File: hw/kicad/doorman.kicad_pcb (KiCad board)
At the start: 2 copper layers, 18 parts, among them J1 Ring Detection, J2 Lock, J3 Power Supply, K1 S1A05, Q1 BC337, SW1 Button, U1 WeMos_mini, U2 PC817

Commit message: New Dorman v 1.0 PCB design.
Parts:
- added H1: MountingHole_2.2mm_M2, MountingHole:MountingHole_2.2mm_M2, F.Cu at (126.0, 117.0)
- added H1: MountingHole_2.2mm_M2, MountingHole:MountingHole_2.2mm_M2, F.Cu at (104.0, 66.0)
- Button: renamed from SW1; footprint Button_Switch_SMD:SW_SPST_EVQP0 -> Connector_PinHeader_2.54mm:PinHeader_1x02_P2.54mm_Vertical
- J1: value Ring Detection -> RDet
- J3: value Power Supply -> PWR
- LockLED: renamed from LED2; value LED Red -> Red
- R1, R2, R3, R4, R5: footprint Resistor_THT:R_Axial_DIN0204_L3.6mm_D1.6mm_P5.08mm_Vertical -> Resistor_THT:R_Axial_DIN0204_L3.6mm_D1.6mm_P7.62mm_Horizontal
- RingLED: renamed from LED1; value LED Green -> Green
- U1: value WeMos_mini -> WeMos_D1_mini
- moved J1 77.2 mm to (111.3, 127.8), turned to 180 degrees
- moved R3 71.6 mm to (108.7, 66.5), turned to 270 degrees
- moved D1 66.3 mm to (109.2, 112.3), turned to 270 degrees
- moved J3 62.8 mm to (113.8, 54.9)
- moved LockLED 57.1 mm to (111.3, 62.7), turned to 180 degrees
- moved JP1 54.1 mm to (108.5, 54.9), turned to 270 degrees
- moved K1 52.7 mm to (122.9, 105.7), turned to 180 degrees
- moved J2 47.7 mm to (119.9, 127.8), turned to 180 degrees
- moved RingLED 41.5 mm to (120.9, 62.7)
- moved U2 41.4 mm to (119.6, 93.0), turned to 90 degrees
- moved D2 41.3 mm to (111.3, 100.3)
- moved R2 40.4 mm to (123.4, 66.5), turned to 270 degrees
- moved R4 32.6 mm to (107.4, 82.8), turned to 270 degrees
- moved Q1 32.4 mm to (112.5, 82.8), turned to 270 degrees
- moved R5 28.5 mm to (115.1, 93.0), turned to 180 degrees
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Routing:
- net GND: track 0.00 -> 126.0 mm
- net +5V: track 0.00 -> 59.0 mm
- net PhGND: track 0.00 -> 56.3 mm
- net Net-(D2-Pad2): track 0.00 -> 54.9 mm
- net PhLock: track 0.00 -> 40.0 mm
- net Net-(D1-Pad1): track 0.00 -> 27.7 mm
- net Net-(R2-Pad2): track 0.00 -> 26.7 mm
- net Butt: track 0.00 -> 24.1 mm
- net PhRing: track 0.00 -> 10.4 mm
- net +3V3: track 0.00 -> 9.67 mm
- net Net-(Q1-Pad2): track 0.00 -> 6.13 mm
- net Net-(J3-Pad1): track 0.00 -> 5.33 mm
- net Net-(LED2-Pad2): track 0.00 -> 3.81 mm
- net Net-(LED1-Pad2): track 0.00 -> 3.81 mm
- net RingDet: track 0.00 -> 3.81 mm
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- added copper zone on F.Cu, net GND
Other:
- board outline added: 28 x 80 mm
- net class My added: clearance 0.2, trace_width 0.35, via_dia 0.8, via_drill 0.4
- board text added: "+"
- board text added: "-"
- board text added: "Doorman HomeKit"
- board text added: "Ext PWR"
- board text added: "Lock"
- board text added: "Only +5V"
- board text added: "RingDet"
- board text added: "version 1.0"
- board text added: "zokl@2020"

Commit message: PCB Update.
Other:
- net class My removed
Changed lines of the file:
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@@
     (visible_elements FFFFFF7F)
     (pcbplotparams
-      (layerselection 0x010fc_ffffffff)
+      (layerselection 0x010a0_7fffffff)
       (usegerberextensions false)
       (usegerberattributes false)
@@
       (padsonsilk false)
       (subtractmaskfromsilk false)
-      (outputformat 1)
+      (outputformat 4)
       (mirror false)
-      (drillshape 1)
+      (drillshape 0)
       (scaleselection 1)
       (outputdirectory ""))
@@
     (add_net PhRing)
     (add_net RingDet)
-  )
-  (net_class My ""
-    (clearance 0.2)
-    (trace_width 0.35)
-    (via_dia 0.8)
-    (via_drill 0.4)
-    (uvia_dia 0.3)
-    (uvia_drill 0.1)
   )
   (module Package_TO_SOT_THT:TO-92_Inline_Wide (layer F.Cu)
@@
     (connect_pads (clearance 0.508))
     (min_thickness 0.254)
-    (fill (arc_segments 32) (thermal_gap 0.508) (thermal_bridge_width 0.508))
+    (fill yes (arc_segments 32) (thermal_gap 0.508) (thermal_bridge_width 0.508))
     (polygon
       (pts

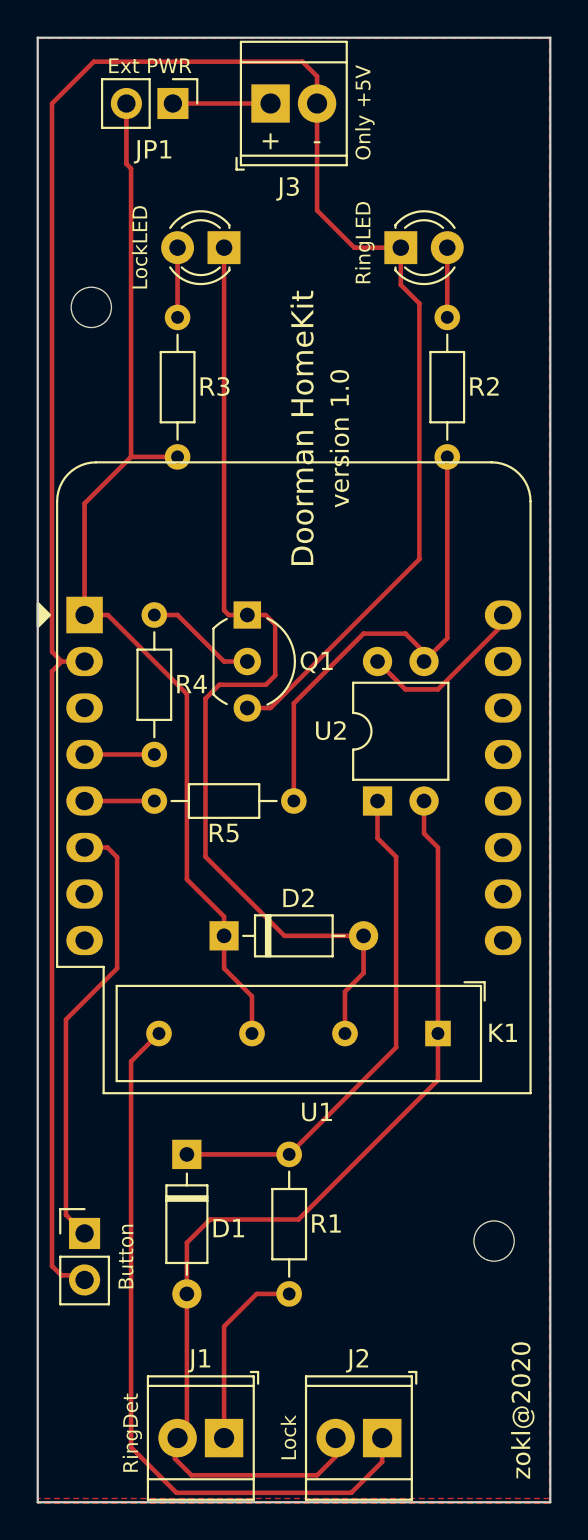
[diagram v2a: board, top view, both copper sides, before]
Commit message: New PCB mask, new PWR wires size.
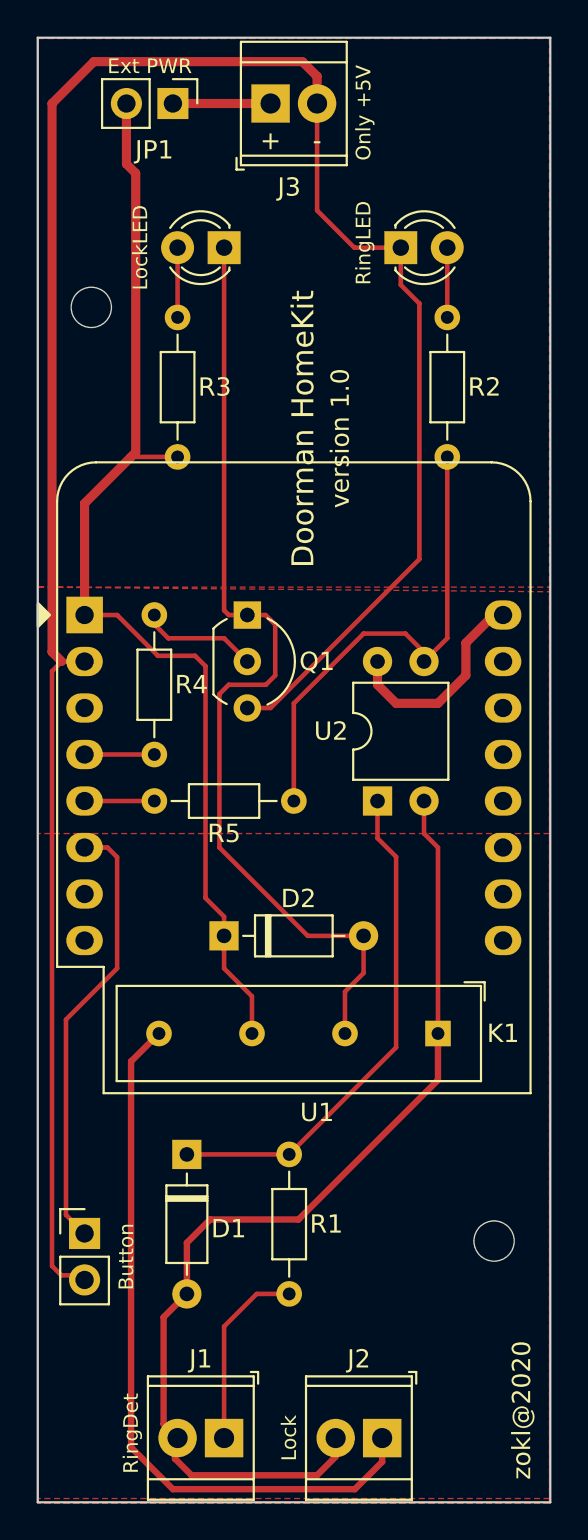
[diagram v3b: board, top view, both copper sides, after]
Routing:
- net +3V3: track 9.67 -> 11.8 mm
- net +5V: track 59.0 -> 60.7 mm
- net Net-(D2-Pad2): track 54.9 -> 53.2 mm

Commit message: Final PCB.
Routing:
- net +5V: track 60.7 -> 61.7 mm
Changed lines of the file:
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@@
-(kicad_pcb (version 20171130) (host pcbnew "(5.1.5-0-10_14)")
+(kicad_pcb (version 20171130) (host pcbnew 5.1.5-52549c5~84~ubuntu18.04.1)
   (general
     (thickness 1.6)
     (drawings 19)
-    (tracks 112)
+    (tracks 115)
     (zones 0)
     (modules 20)
@@
     (last_trace_width 0.25)
     (trace_clearance 0.2)
-    (zone_clearance 0.508)
+    (zone_clearance 0.48)
     (zone_45_only no)
     (trace_min 0.2)
@@
     (solder_mask_min_width 0.25)
     (aux_axis_origin 0 0)
+    (grid_origin 101.072 51.27)
     (visible_elements FFFFFF7F)
     (pcbplotparams
@@
   (segment (start 111.252 100.33) (end 111.252 102.108) (width 0.25) (layer F.Cu) (net 4))
   (segment (start 111.252 102.108) (end 112.776 103.632) (width 0.25) (layer F.Cu) (net 4))
-  (segment (start 106.172 74.168) (end 108.712 74.168) (width 0.25) (layer F.Cu) (net 4))
-  (segment (start 103.632 76.708) (end 106.172 74.168) (width 0.5) (layer F.Cu) (net 4))
-  (segment (start 103.632 82.804) (end 103.632 76.708) (width 0.5) (layer F.Cu) (net 4))
-  (segment (start 106.426 73.914) (end 106.172 74.168) (width 0.5) (layer F.Cu) (net 4))
-  (segment (start 106.426 58.674) (end 106.426 73.914) (width 0.5) (layer F.Cu) (net 4))
-  (segment (start 105.918 58.166) (end 106.426 58.674) (width 0.5) (layer F.Cu) (net 4))
-  (segment (start 105.918 54.864) (end 105.918 58.166) (width 0.5) (layer F.Cu) (net 4))
+  (segment (start 107.188 64.262) (end 107.188 73.152) (width 0.5) (layer F.Cu) (net 4))
+  (segment (start 105.918 62.992) (end 107.188 64.262) (width 0.5) (layer F.Cu) (net 4))
+  (segment (start 105.918 54.864) (end 105.918 62.992) (width 0.5) (layer F.Cu) (net 4))
+  (segment (start 107.188 73.914) (end 107.188 73.152) (width 0.5) (layer F.Cu) (net 4))
+  (segment (start 108.458 74.422) (end 108.712 74.168) (width 0.25) (layer F.Cu) (net 4))
+  (segment (start 107.188 74.422) (end 108.458 74.422) (width 0.25) (layer F.Cu) (net 4))
+  (segment (start 107.188 73.914) (end 107.188 74.422) (width 0.25) (layer F.Cu) (net 4))
+  (segment (start 107.188 80.518) (end 107.188 73.914) (width 0.5) (layer F.Cu) (net 4))
+  (segment (start 104.902 82.804) (end 107.188 80.518) (width 0.5) (layer F.Cu) (net 4))
+  (segment (start 103.632 82.804) (end 104.902 82.804) (width 0.5) (layer F.Cu) (net 4))
   (segment (start 111.252 99.28) (end 111.252 100.33) (width 0.25) (layer F.Cu) (net 4))
+  (segment (start 110.236 98.264) (end 111.252 99.28) (width 0.25) (layer F.Cu) (net 4))
+  (segment (start 104.648 82.804) (end 106.87601 85.03201) (width 0.25) (layer F.Cu) (net 4))
   (segment (start 110.236 85.598) (end 110.236 98.264) (width 0.25) (layer F.Cu) (net 4))
-  (segment (start 110.236 98.264) (end 111.252 99.28) (width 0.25) (layer F.Cu) (net 4))
-  (segment (start 103.632 82.804) (end 105.41 82.804) (width 0.25) (layer F.Cu) (net 4))
-  (segment (start 107.63801 85.03201) (end 109.67001 85.03201) (width 0.25) (layer F.Cu) (net 4))
-  (segment (start 105.41 82.804) (end 107.63801 85.03201) (width 0.25) (layer F.Cu) (net 4))
+  (segment (start 106.87601 85.03201) (end 109.67001 85.03201) (width 0.25) (layer F.Cu) (net 4))
   (segment (start 109.67001 85.03201) (end 110.236 85.598) (width 0.25) (layer F.Cu) (net 4))
+  (segment (start 103.632 82.804) (end 104.648 82.804) (width 0.25) (layer F.Cu) (net 4))
   (segment (start 113.03 119.888) (end 114.808 119.888) (width 0.25) (layer F.Cu) (net 5))
   (segment (start 111.252 121.666) (end 113.03 119.888) (width 0.25) (layer F.Cu) (net 5))
@@
   (segment (start 126.492 82.804) (end 125.984 82.804) (width 0.5) (layer F.Cu) (net 16))
   (zone (net 7) (net_name GND) (layer F.Cu) (hatch edge 0.508)
-    (connect_pads (clearance 0.508))
+    (connect_pads (clearance 0.48))
     (min_thickness 0.254)
-    (fill (arc_segments 32) (thermal_gap 0.508) (thermal_bridge_width 0.508))
+    (fill yes (arc_segments 32) (thermal_gap 0.48) (thermal_bridge_width 0.48))
     (polygon
       (pts
-        (xy 129.032 131.064) (xy 101.092 131.064) (xy 101.092 51.308) (xy 129.032 51.308)
+        (xy 129.072 131.27) (xy 101.072 131.27) (xy 101.072 81.67) (xy 129.072 81.67)
       )
     )
-  )
-  (zone (net 7) (net_name GND) (layer F.Cu) (hatch edge 0.508)
-    (connect_pads (clearance 0.508))
-    (min_thickness 0.254)
-    (fill (arc_segments 32) (thermal_gap 0.508) (thermal_bridge_width 0.508))
-    (polygon
-      (pts
-        (xy 129.032 131.318) (xy 101.092 131.318) (xy 101.092 51.308) (xy 129.032 51.308)
-      )
-    )
-  )
-  (zone (net 7) (net_name GND) (layer F.Cu) (hatch edge 0.508)
-    (connect_pads (clearance 0.508))
-    (min_thickness 0.254)
-    (fill (arc_segments 32) (thermal_gap 0.508) (thermal_bridge_width 0.508))
-    (polygon
-      (pts
-        (xy 129.032 131.318) (xy 101.092 131.318) (xy 101.092 51.308) (xy 129.032 51.308)
-      )
-    )
-  )
-  (zone (net 7) (net_name GND) (layer F.Cu) (hatch edge 0.508)
-    (connect_pads (clearance 0.508))
-    (min_thickness 0.254)
-    (fill (arc_segments 32) (thermal_gap 0.508) (thermal_bridge_width 0.508))
-    (polygon
-      (pts
-        (xy 129.032 94.742) (xy 101.092 94.742) (xy 101.092 81.28) (xy 129.032 81.28)
-      )
-    )
-  )
-  (zone (net 7) (net_name GND) (layer F.Cu) (hatch edge 0.508)
-    (connect_pads (clearance 0.508))
-    (min_thickness 0.254)
-    (fill yes (arc_segments 32) (thermal_gap 0.508) (thermal_bridge_width 0.508))
-    (polygon
-      (pts
-        (xy 129.032 81.534) (xy 129.032 131.318) (xy 101.092 131.318) (xy 101.092 81.28)
-      )
-    )

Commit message: PCB production documentation
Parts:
- removed the H1 at (126.0, 117.0)
- removed the H1 at (104.0, 66.0)
- added H1: MountingHole_Pad, MountingHole:MountingHole_2.2mm_M2_Pad, F.Cu at (126.0, 117.0)
- added H2: MountingHole_Pad, MountingHole:MountingHole_2.2mm_M2_Pad, F.Cu at (104.0, 66.0)
- J1: value RDet -> Ring Detection
- J3: value PWR -> Power Supply
- renumbered RingLED to LED1, LockLED to LED2, Button to SW1
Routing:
- net GND: track 126.0 -> 128.1 mm
- added copper zone on B.Cu, net GND
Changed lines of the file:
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@@
     (thickness 1.6)
     (drawings 19)
-    (tracks 115)
+    (tracks 118)
     (zones 0)
     (modules 20)
@@
     (add_net RingDet)
   )
+  (module MountingHole:MountingHole_2.2mm_M2_Pad (layer F.Cu)
+    (at 104 66)
+    (descr "Mounting Hole 2.2mm, M2")
+    (tags "mounting hole 2.2mm m2")
+    (attr virtual)
+    (fp_text reference H2 (at 0 -3.2) (layer F.SilkS) hide
+      (effects (font (size 1 1) (thickness 0.15)))
+    )
+    (fp_text value MountingHole_Pad (at 0 3.2) (layer F.Fab)
+      (effects (font (size 1 1) (thickness 0.15)))
+    )
+    (fp_circle (center 0 0) (end 2.45 0) (layer F.CrtYd) (width 0.05))
+    (fp_circle (center 0 0) (end 2.2 0) (layer Cmts.User) (width 0.15))
+    (fp_text user %R (at 0.3 0) (layer F.Fab)
+      (effects (font (size 1 1) (thickness 0.15)))
+    )
+    (pad 1 thru_hole circle (at 0 0) (size 4.4 4.4) (drill 2.2) (layers *.Cu *.Mask)
+      (net 7 GND))
+  )
+  (module MountingHole:MountingHole_2.2mm_M2_Pad (layer F.Cu)
+    (at 126 117)
+    (descr "Mounting Hole 2.2mm, M2")
+    (tags "mounting hole 2.2mm m2")
+    (zone_connect 2)
+    (attr virtual)
+    (fp_text reference H1 (at 0 -3.2) (layer F.SilkS) hide
+      (effects (font (size 1 1) (thickness 0.15)))
+    )
+    (fp_text value MountingHole_Pad (at 0 3.2) (layer F.Fab)
+      (effects (font (size 1 1) (thickness 0.15)))
+    )
+    (fp_circle (center 0 0) (end 2.45 0) (layer F.CrtYd) (width 0.05))
+    (fp_circle (center 0 0) (end 2.2 0) (layer Cmts.User) (width 0.15))
+    (fp_text user %R (at 0.3 0) (layer F.Fab)
+      (effects (font (size 1 1) (thickness 0.15)))
+    )
+    (pad 1 thru_hole circle (at 0 0) (size 4.4 4.4) (drill 2.2) (layers *.Cu *.Mask)
+      (net 7 GND) (zone_connect 2))
+  )
   (module Package_TO_SOT_THT:TO-92_Inline_Wide (layer F.Cu)
     (at 112.522 82.804 270)
@@
     )
   )
-  (module MountingHole:MountingHole_2.2mm_M2 locked (layer F.Cu)
-    (at 126 117)
-    (descr "Mounting Hole 2.2mm, no annular, M2")
-    (tags "mounting hole 2.2mm no annular m2")
-    (attr virtual)
-    (fp_text reference H1 (at 0 -3.2) (layer F.SilkS) hide
-      (effects (font (size 1 1) (thickness 0.15)))
-    )
-    (fp_text value MountingHole_2.2mm_M2 (at 0 3.2) (layer F.Fab) hide
-      (effects (font (size 1 1) (thickness 0.15)))
-    )
-    (fp_text user %R (at 0.3 0) (layer F.Fab)
-      (effects (font (size 1 1) (thickness 0.15)))
-    )
-    (fp_circle (center 0 0) (end 2.2 0) (layer Cmts.User) (width 0.15))
-    (fp_circle (center 0 0) (end 2.45 0) (layer F.CrtYd) (width 0.05))
-    (pad 1 np_thru_hole circle (at 0 0) (size 2.2 2.2) (drill 2.2) (layers *.Cu *.Mask))
-  )
-  (module MountingHole:MountingHole_2.2mm_M2 locked (layer F.Cu)
-    (at 104 66)
-    (descr "Mounting Hole 2.2mm, no annular, M2")
-    (tags "mounting hole 2.2mm no annular m2")
-    (attr virtual)
-    (fp_text reference H1 (at 0 -3.2) (layer F.SilkS) hide
-      (effects (font (size 1 1) (thickness 0.15)))
-    )
-    (fp_text value MountingHole_2.2mm_M2 (at 0 3.2) (layer F.Fab) hide
-      (effects (font (size 1 1) (thickness 0.15)))
-    )
-    (fp_circle (center 0 0) (end 2.45 0) (layer F.CrtYd) (width 0.05))
-    (fp_circle (center 0 0) (end 2.2 0) (layer Cmts.User) (width 0.15))
-    (fp_text user %R (at 0.3 0) (layer F.Fab)
-      (effects (font (size 1 1) (thickness 0.15)))
-    )
-    (pad 1 np_thru_hole circle (at 0 0) (size 2.2 2.2) (drill 2.2) (layers *.Cu *.Mask))
-  )
   (module Resistor_THT:R_Axial_DIN0204_L3.6mm_D1.6mm_P7.62mm_Horizontal (layer F.Cu)
     (at 115.062 92.964 180)
@@
     (descr "Through hole straight pin header, 1x02, 2.54mm pitch, single row")
     (tags "Through hole pin header THT 1x02 2.54mm single row")
-    (fp_text reference Button (at 2.286 1.27 90) (layer F.SilkS)
+    (fp_text reference SW1 (at 2.286 1.27 90) (layer F.SilkS)
       (effects (font (size 0.8 0.8) (thickness 0.2)))
     )
@@
     (descr "LED, diameter 3.0mm, 2 pins")
     (tags "LED diameter 3.0mm 2 pins")
-    (fp_text reference LockLED (at 4.572 0 90) (layer F.SilkS)
+    (fp_text reference LED2 (at 4.572 0 90) (layer F.SilkS)
       (effects (font (size 0.8 0.8) (thickness 0.2)))
     )
@@
     (descr "LED, diameter 3.0mm, 2 pins")
     (tags "LED diameter 3.0mm 2 pins")
-    (fp_text reference RingLED (at -2.032 -0.254 90) (layer F.SilkS)
+    (fp_text reference LED1 (at -2.032 -0.254 90) (layer F.SilkS)
       (effects (font (size 0.8 0.8) (thickness 0.2)))
     )
@@
       (effects (font (size 1 1) (thickness 0.15)))
     )
-    (fp_text value PWR (at 1.27 4.37) (layer F.Fab)
+    (fp_text value "Power Supply" (at 1.27 4.37) (layer F.Fab)
       (effects (font (size 1 1) (thickness 0.15)))
     )
@@
       (effects (font (size 1 1) (thickness 0.15)))
     )
-    (fp_text value RDet (at 1.27 4.37) (layer F.Fab)
+    (fp_text value "Ring Detection" (at 1.27 4.37) (layer F.Fab)
       (effects (font (size 1 1) (thickness 0.15)))
     )
@@
     )
   )
+  (gr_line (start 129.072 131.27) (end 129.072 51.27) (layer Edge.Cuts) (width 0.12))
   (gr_text RingDet (at 106.172 127.508 90) (layer F.SilkS)
     (effects (font (size 0.8 0.8) (thickness 0.2)))
@@
   (gr_line (start 101.072 51.27) (end 101.072 131.27) (layer Edge.Cuts) (width 0.12))
   (gr_line (start 129.072 51.27) (end 101.072 51.27) (layer Edge.Cuts) (width 0.12))
-  (gr_line (start 129.072 131.27) (end 129.072 51.27) (layer Edge.Cuts) (width 0.12))
   (gr_line (start 101.072 131.27) (end 129.072 131.27) (layer Edge.Cuts) (width 0.12))
   (gr_line (start 100 50) (end 100 133) (layer Margin) (width 0.12))
@@
   (segment (start 102.362 118.872) (end 103.378 118.872) (width 0.25) (layer F.Cu) (net 7))
   (segment (start 102.382 85.344) (end 101.854 85.872) (width 0.25) (layer F.Cu) (net 7))
-  (segment (start 101.854 54.864) (end 101.854 84.816) (width 0.5) (layer F.Cu) (net 7))
   (segment (start 116.332 53.379076) (end 115.530924 52.578) (width 0.5) (layer F.Cu) (net 7))
   (segment (start 115.530924 52.578) (end 104.14 52.578) (width 0.5) (layer F.Cu) (net 7))
@@
   (segment (start 121.92 65.786) (end 120.904 64.77) (width 0.25) (layer F.Cu) (net 7))
   (segment (start 112.522 87.884) (end 113.792 87.884) (width 0.25) (layer F.Cu) (net 7))
+  (segment (start 101.942 66) (end 101.872 66.07) (width 0.25) (layer F.Cu) (net 7))
+  (segment (start 104 66) (end 101.942 66) (width 0.25) (layer F.Cu) (net 7))
+  (segment (start 101.854 54.864) (end 101.872 66.07) (width 0.5) (layer F.Cu) (net 7))
+  (segment (start 101.872 66.07) (end 101.854 84.816) (width 0.5) (layer F.Cu) (net 7))
   (segment (start 113.792 54.864) (end 108.458 54.864) (width 0.5) (layer F.Cu) (net 8))
   (segment (start 123.444 66.548) (end 123.444 62.738) (width 0.25) (layer F.Cu) (net 9))
@@
     (connect_pads (clearance 0.48))
     (min_thickness 0.254)
+    (fill yes (arc_segments 32) (thermal_gap 0.48) (thermal_bridge_width 0.48))
+    (polygon
+      (pts
+        (xy 129.072 131.27) (xy 101.072 131.27) (xy 101.072 81.67) (xy 129.072 81.67)
+      )
+    )
+  )
+  (zone (net 7) (net_name GND) (layer B.Cu) (hatch edge 0.508)
+    (connect_pads (clearance 0.48))
+    (min_thickness 0.254)
